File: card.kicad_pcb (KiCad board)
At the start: 2 copper layers, 85.6 x 54 mm, 53 parts

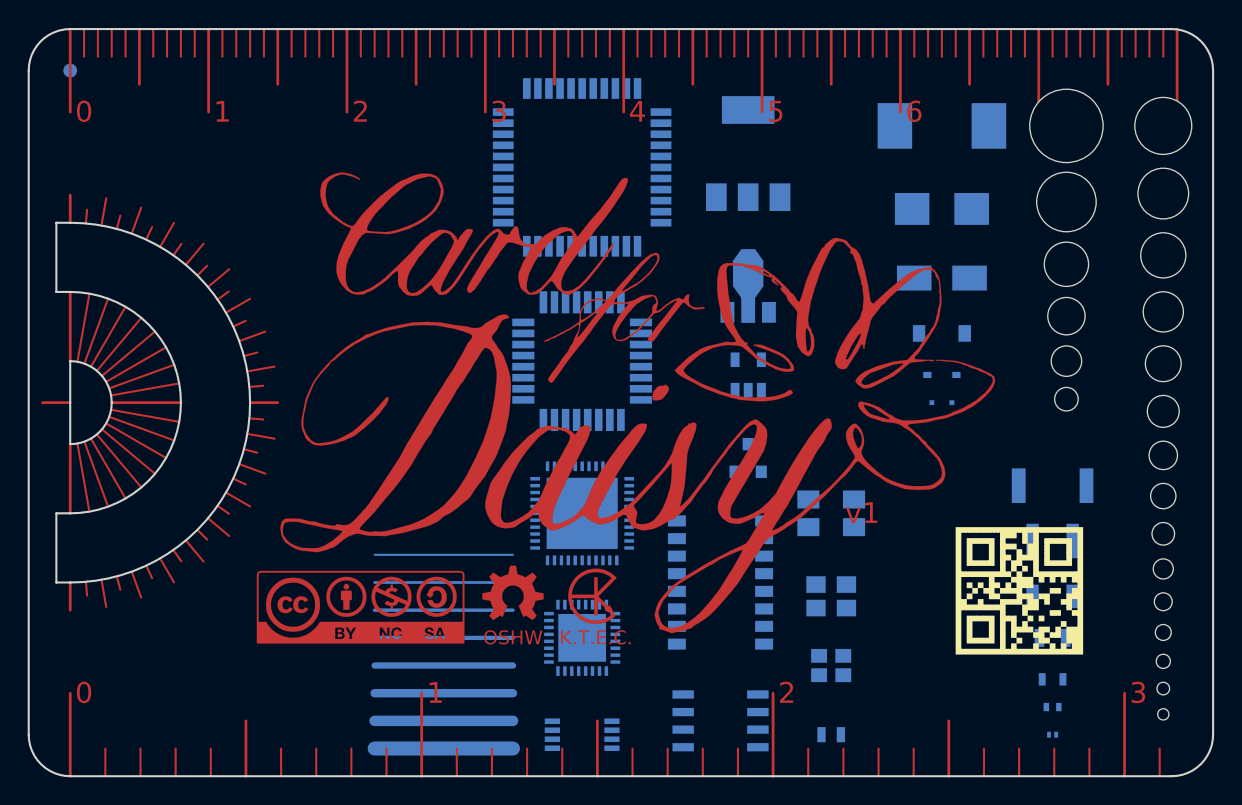
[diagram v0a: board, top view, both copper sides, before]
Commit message: Design v2 - Contract logo mask - Add scale numbers to protractor - Some miner fixes
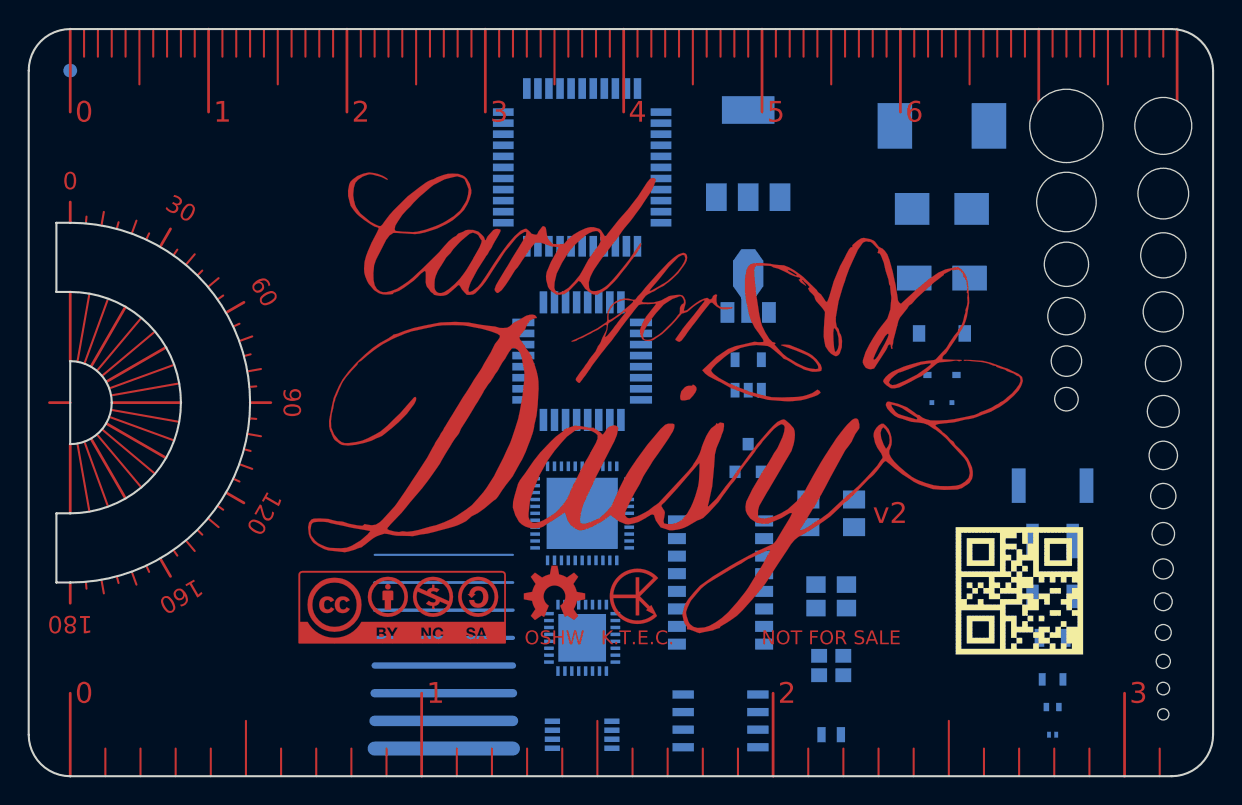
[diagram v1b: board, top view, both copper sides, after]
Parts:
- moved LOGO2 3.00 mm to (74.0, 71.0)
- moved LOGO3 3.00 mm to (68.0, 71.0)
- moved LOGO4 3.00 mm to (57.0, 72.0)
- moved LOGO1 2.00 mm to (76.0, 57.0)
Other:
- board text added: "0"
- board text added: "120"
- board text added: "160"
- board text added: "180"
- board text added: "30"
- board text added: "90"
- board text added: "NOT FOR SALE"
- board text added: "v2"
- board text removed: "v1"

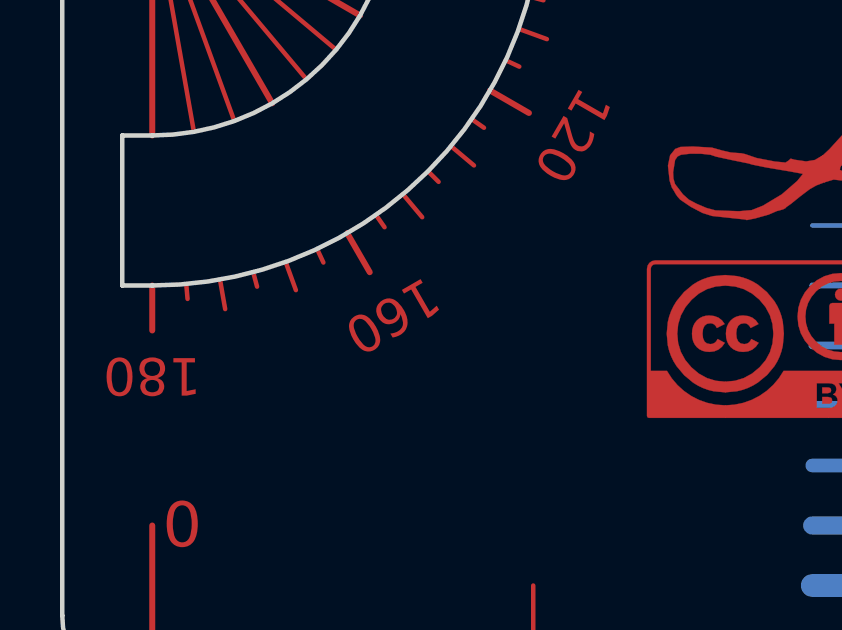
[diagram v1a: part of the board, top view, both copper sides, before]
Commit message: Fix minor typo: 160 to 150
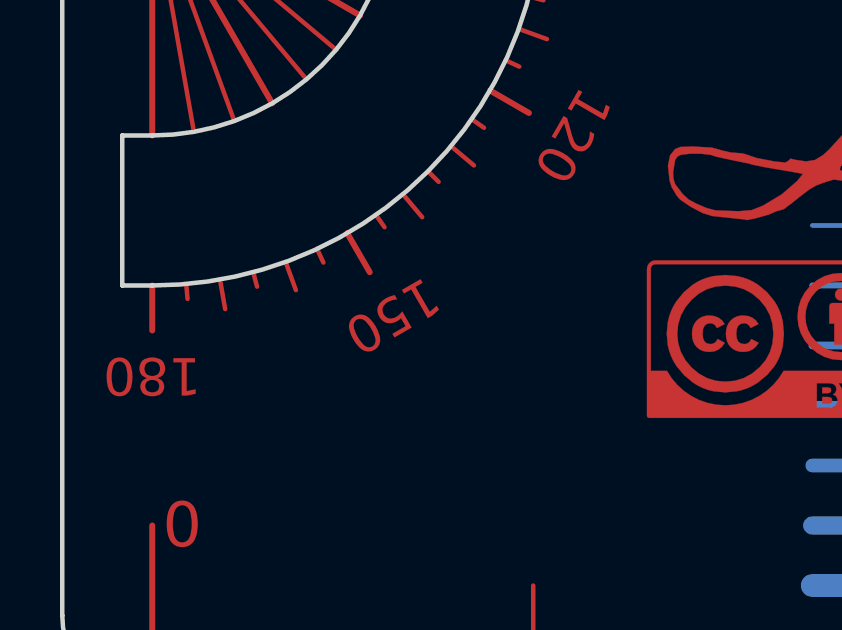
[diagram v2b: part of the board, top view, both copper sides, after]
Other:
- board text added: "150"
- board text removed: "160"
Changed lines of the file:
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@@
-(kicad_pcb (version 4) (host pcbnew 4.0.2-stable)
+(kicad_pcb (version 4) (host pcbnew 4.0.6)
   (general
     (links 0)
@@
     (effects (font (size 1.25 1.25) (thickness 0.2)))
   )
-  (gr_text 160 (at 41 71 210) (layer F.Mask)
+  (gr_text 150 (at 41 71 210) (layer F.Mask)
     (effects (font (size 1.25 1.25) (thickness 0.2)))
   )
@@
     (effects (font (size 1.25 1.25) (thickness 0.2)))
   )
-  (gr_text 160 (at 41 71 210) (layer F.Cu)
+  (gr_text 150 (at 41 71 210) (layer F.Cu)
     (effects (font (size 1.25 1.25) (thickness 0.2)))
   )

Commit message: v3
hide 7
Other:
- board text added: "v3"
- board text removed: "v2"
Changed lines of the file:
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@@
       (effects (font (size 1 1) (thickness 0.15)))
     )
-    (fp_text user 7 (at 71 6) (layer F.Cu)
+    (fp_text user 7 (at 71 6) (layer F.SilkS) hide
       (effects (font (size 1.5 1.5) (thickness 0.2)))
     )
@@
     (effects (font (size 1 1) (thickness 0.15)) (justify mirror))
   )
-  (gr_text v2 (at 91 65) (layer F.Cu)
+  (gr_text v3 (at 91 65) (layer F.Cu)
     (effects (font (size 1.5 1.5) (thickness 0.2)) (justify left))
   )

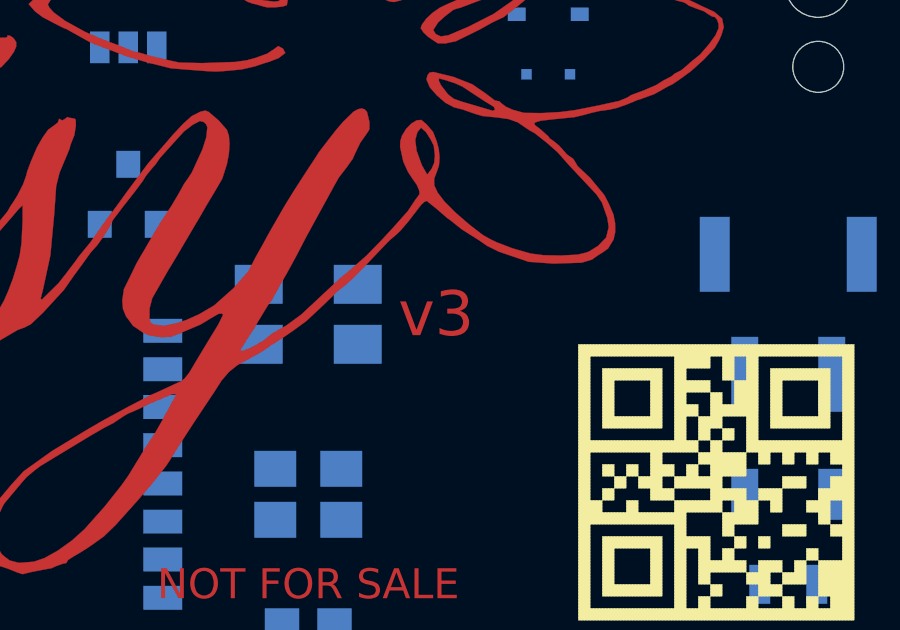
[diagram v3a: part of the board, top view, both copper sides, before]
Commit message: Design v4 - Add lost Text Size label back - Minor fixes
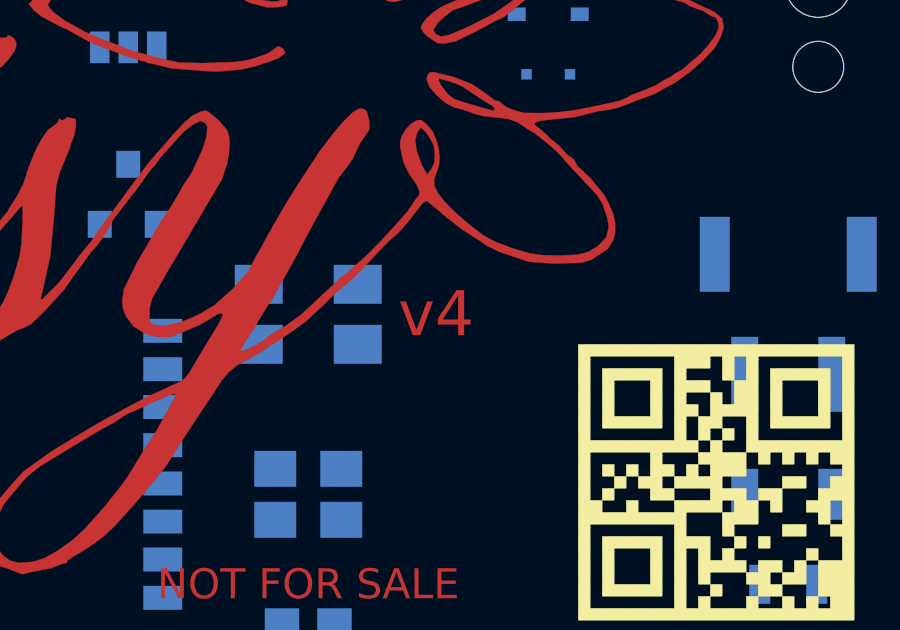
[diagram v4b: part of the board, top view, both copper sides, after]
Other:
- board text added: "Text Size (thickness)"
- board text added: "v4"
- board text removed: "v3"
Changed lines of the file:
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@@
-(kicad_pcb (version 4) (host pcbnew 4.0.6)
+(kicad_pcb (version 4) (host pcbnew 4.0.2-stable)
   (general
     (links 0)
     (no_connects 0)
-    (area 29.924999 29.924999 115.675001 84.075001)
+    (area 14.629761 25.15 115.675001 85.975)
     (thickness 1.6)
     (drawings 80)
@@
   (title_block
     (title "Daisy Card")
-    (date 2017-08-18)
-    (rev v2)
+    (date 2017-09-04)
+    (rev v4)
     (company K.T.E.C.)
   )
@@
     (fp_line (start -2.954422 -0.52094) (end -7.878462 -1.38919) (layer F.Cu) (width 0.15))
   )
+  (gr_text "Text Size\n(thickness)" (at 51 68) (layer B.SilkS)
+    (effects (font (size 1 1) (thickness 0.2)) (justify left mirror))
+  )
   (gr_text "NOT FOR SALE" (at 88 74) (layer F.Cu)
     (effects (font (size 1 1) (thickness 0.2)))
@@
     (effects (font (size 1 1) (thickness 0.15)) (justify mirror))
   )
-  (gr_text v3 (at 91 65) (layer F.Cu)
+  (gr_text v4 (at 91 65) (layer F.Cu)
     (effects (font (size 1.5 1.5) (thickness 0.2)) (justify left))
   )
@@
   (gr_arc (start 33 81) (end 33 84) (angle 90) (layer Edge.Cuts) (width 0.15))
   (gr_arc (start 33 33) (end 30 33) (angle 90) (layer Edge.Cuts) (width 0.15))
-  (dimension 5 (width 0.3) (layer Eco1.User)
-    (gr_text "5.000 mm" (at 43.5 69.35) (layer Eco1.User)
-      (effects (font (size 1.5 1.5) (thickness 0.3)))
-    )
-    (feature1 (pts (xy 46 57) (xy 46 70.7)))
-    (feature2 (pts (xy 41 57) (xy 41 70.7)))
-    (crossbar (pts (xy 41 68) (xy 46 68)))
-    (arrow1a (pts (xy 46 68) (xy 44.873496 68.586421)))
-    (arrow1b (pts (xy 46 68) (xy 44.873496 67.413579)))
-    (arrow2a (pts (xy 41 68) (xy 42.126504 68.586421)))
-    (arrow2b (pts (xy 41 68) (xy 42.126504 67.413579)))
-  )
   (gr_text 40 (at 39 81) (layer B.SilkS)
     (effects (font (size 1.016 1.016) (thickness 0.254)) (justify mirror))
